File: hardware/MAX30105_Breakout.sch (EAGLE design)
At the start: 26 parts, among them Q1 200mA/50V, Q2 200mA/50V, U1 1.8V/100mA, U2 MAX30105

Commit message: Fixes from QC check.
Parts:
- added TP1: 1.8V Test, SparkFun-Passives:TEST-POINT3X4
- JP2: value INT-Pullup -> INT
- JP3: value I2C Pull Ups -> PU
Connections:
- net 1.8V: now also TP1.1
- net SCL: now also J2.1; no longer J2.2
- net SDA: now also J2.2; no longer J2.1
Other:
- note added: "5V Only"
- note added: "Clear Jumper to remove I2C Pull-ups from bus"
- note added: "Clear Jumper to remove pull-up from INT"
- note added: "Interface and Logic Conversion"
- note added: "Sensor"
- note added: "Voltage Regulation"
- moved on the sheet: J2, JP2, JP3, Q1, Q2, R1, R2, R5, R8, R9, U2

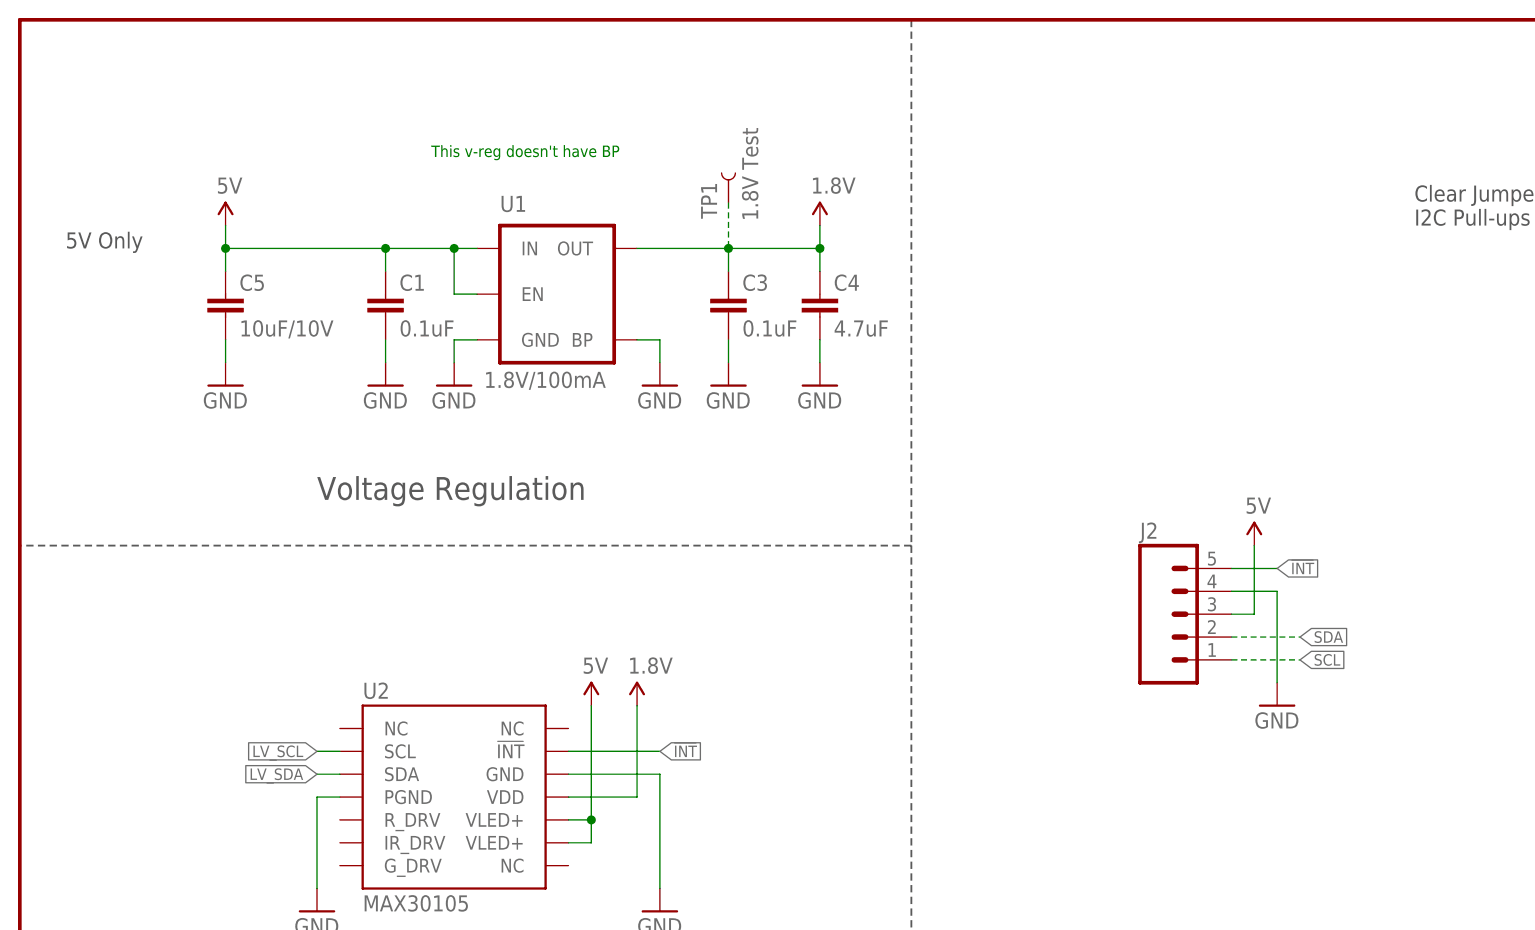
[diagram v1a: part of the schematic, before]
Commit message: Mostly cosmetic changes from review.
Added text to schematic. Changed drill hits to 0.015. Reduced paste pads
to 75% (roughly) on IC.  Created library with only sensor FP.
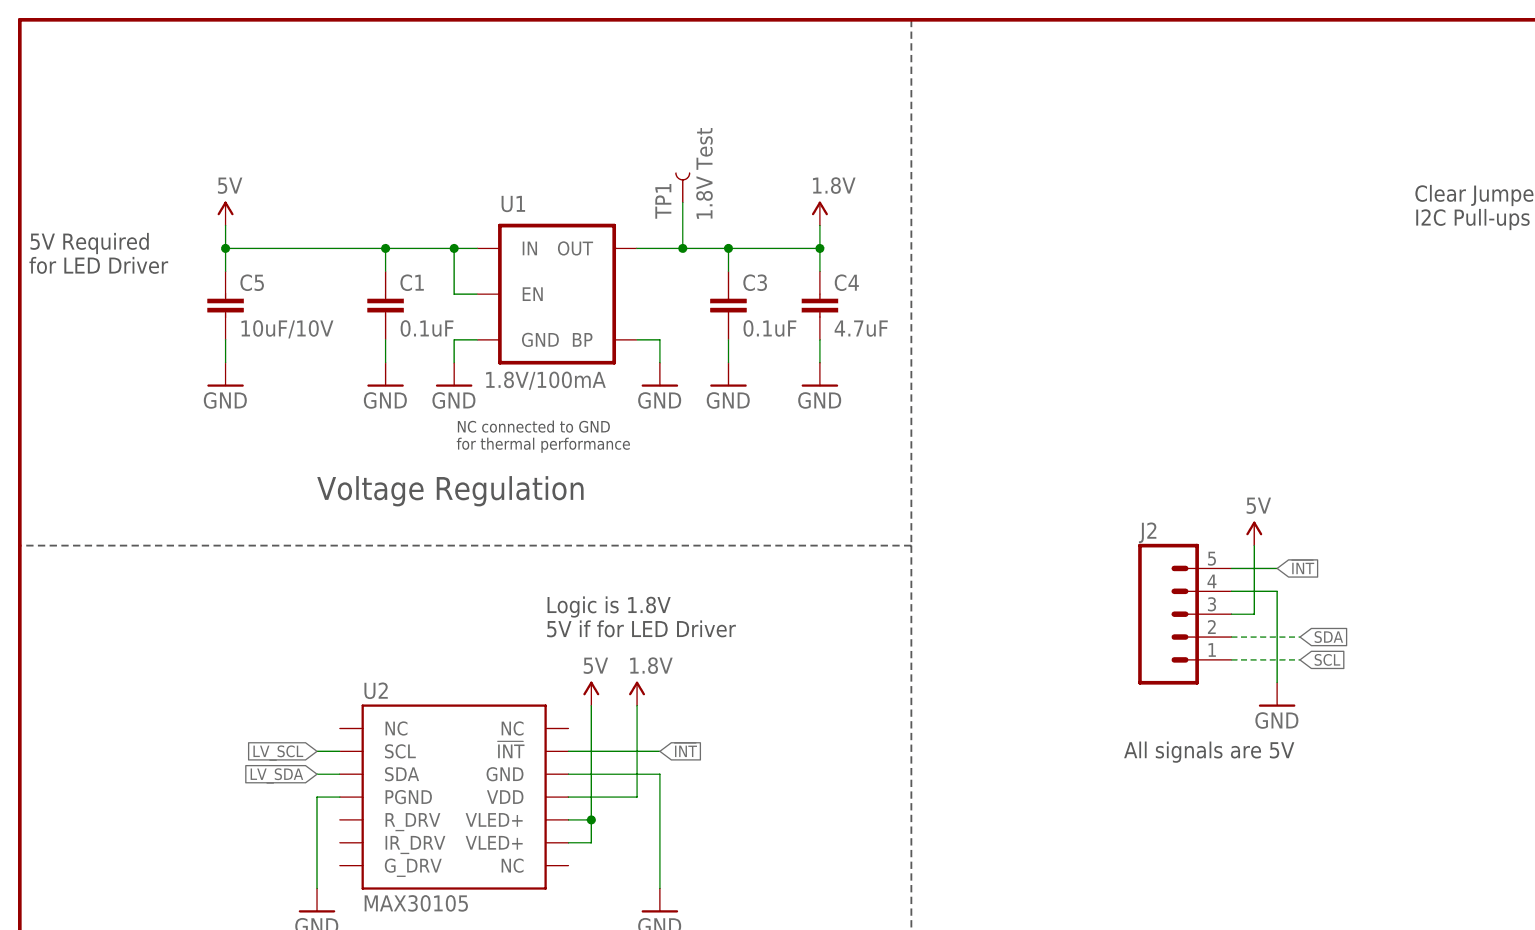
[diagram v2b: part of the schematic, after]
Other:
- note added: "5V Required for LED Driver"
- note added: "All signals are 5V"
- note added: "Logic is 1.8V 5V if for LED Driver"
- note added: "NC connected to GND for thermal performance"
- note removed: "5V Only"
- note removed: "This v-reg doesn't have BP"
- moved on the sheet: TP1

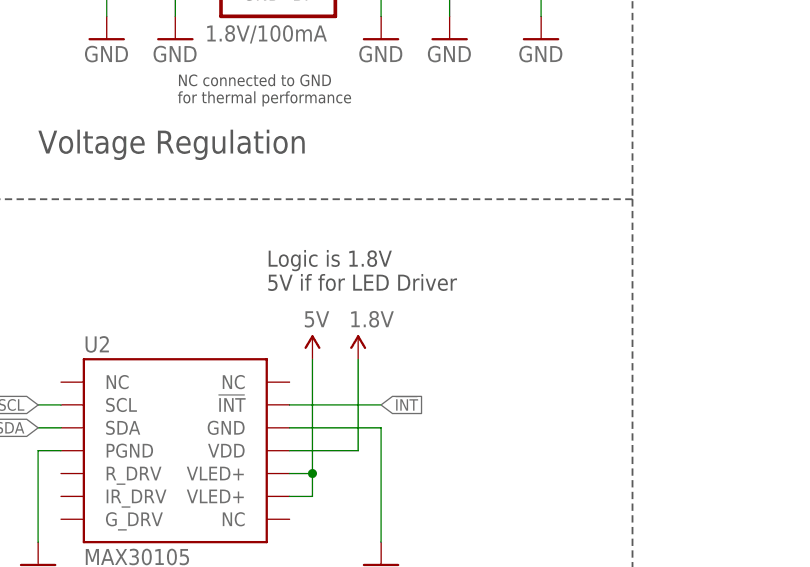
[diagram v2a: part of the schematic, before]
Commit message: Fixed typo in schematic
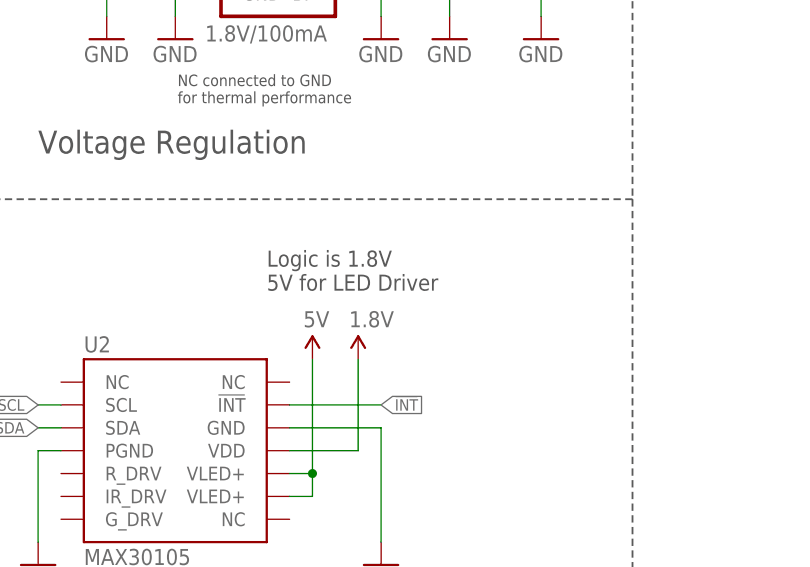
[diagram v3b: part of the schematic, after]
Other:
- note added: "Logic is 1.8V 5V for LED Driver"
- note removed: "Logic is 1.8V 5V if for LED Driver"
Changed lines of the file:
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@@
 pull-up from INT</text>
 <text x="58.42" y="116.84" size="1.778" layer="97">Logic is 1.8V
-5V if for LED Driver</text>
+5V for LED Driver</text>
 <text x="122.682" y="103.378" size="1.778" layer="97">All signals are 5V</text>
 <text x="48.514" y="137.668" size="1.27" layer="97">NC connected to GND

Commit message: Update version to v10
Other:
- note added: "v10"
- note removed: "v01"
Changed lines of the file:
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@@
 <?xml version="1.0" encoding="utf-8"?>
 <!DOCTYPE eagle SYSTEM "eagle.dtd">
-<eagle version="7.6.0">
+<eagle version="7.5.0">
 <drawing>
 <settings>
@@
 <plain>
 <text x="33.02" y="73.66" size="2.54" layer="97">7-Bit I2C: 0x57</text>
-<text x="238.76" y="7.62" size="1.778" layer="94">v01</text>
+<text x="238.76" y="7.62" size="1.778" layer="94">v10</text>
 <text x="170.688" y="11.43" size="2.54" layer="94">N. Seidle</text>
 <wire x1="99.06" y1="185.42" x2="99.06" y2="127" width="0.2032" layer="97" style="longdash"/>
